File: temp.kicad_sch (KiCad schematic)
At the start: 0 parts

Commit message: can transceiver; power; mcu
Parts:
- added C19, C20, C21, C22, C23, C24: 100nF, symbol Device:C
- added D3, D4, D5, D6, D7, D8: BAT54A, Package_TO_SOT_SMD:SOT-23, symbol Diode:BAT54A
- added R53, R55, R57, R59, R61, R63: 680, symbol Device:R
- added R54, R56, R58, R60, R62, R64: 1k, symbol Device:R
- added R65, R66, R67, R68, R69, R70: 10k, symbol Device:R
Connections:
- new net +3.3VA: R53.1, R55.1, R57.1, R59.1, R61.1, R63.1, R65.2, R66.2, R67.2, R68.2, R69.2, R70.2
- new net GNDA: C19.2, C20.2, C21.2, C22.2, C23.2, C24.2
- new net TEMP1: C19.1, R54.2
- new net TEMP2: C20.1, R56.2
- new net TEMP3: C21.1, R58.2
- new net TEMP5: C22.1, R60.2
- new net TEMP6: C23.1, R62.2
- new net TEMP7: C24.1, R64.2
- new net TEMP_HOT: D3.3, D4.3, D5.3, D6.3, D7.3, D8.3, R65.1, R66.1, R67.1, R68.1, R69.1, R70.1
- new net TENSE3: D4.2
- new net TENSE6: D7.2
- new net TSENSE1: D3.1, R53.2, R54.1
- new net TSENSE2: D3.2, D4.1, R55.2, R56.1
- new net TSENSE3: D5.1, R57.2, R58.1
- new net TSENSE4: D5.2, D6.1, R59.2, R60.1
- new net TSENSE5: D6.2, D7.1, R61.2, R62.1
- new net TSENSE6: D8.1, R63.2, R64.1
- new net TSENSE7: D8.2

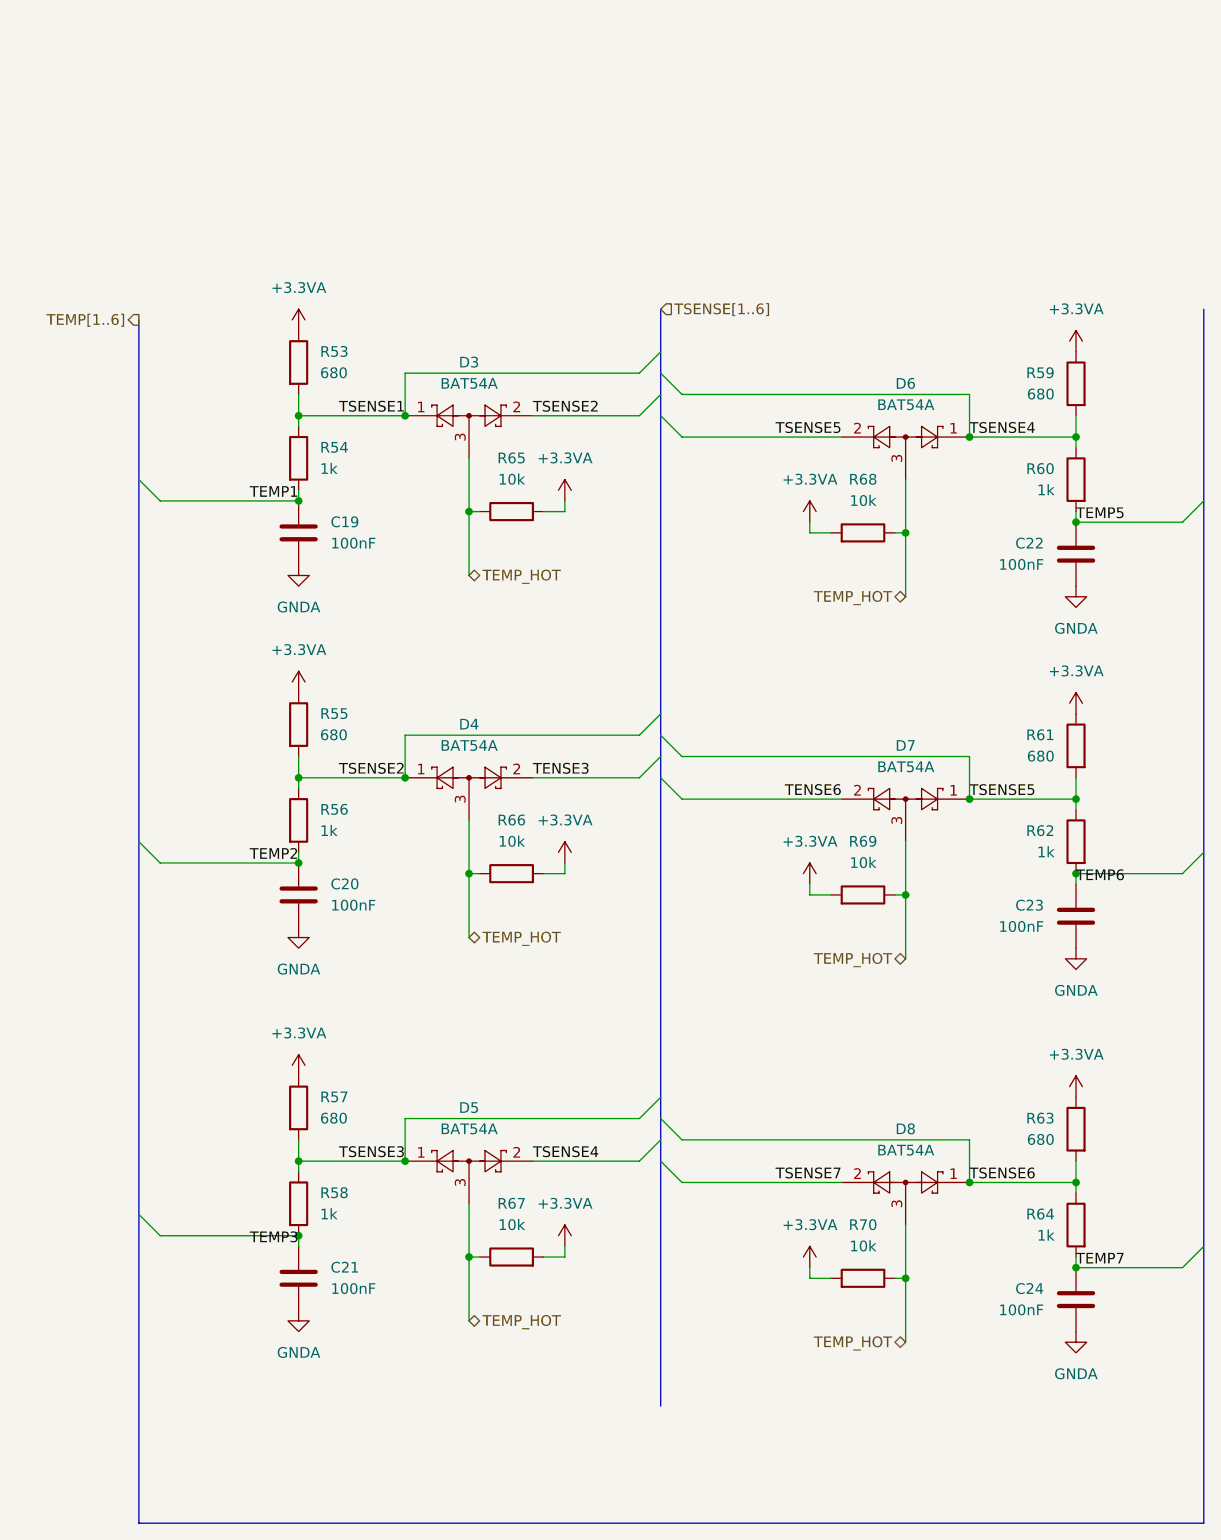
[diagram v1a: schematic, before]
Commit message: Add presentation (slides, PDF, pptx) and latest schematic edits
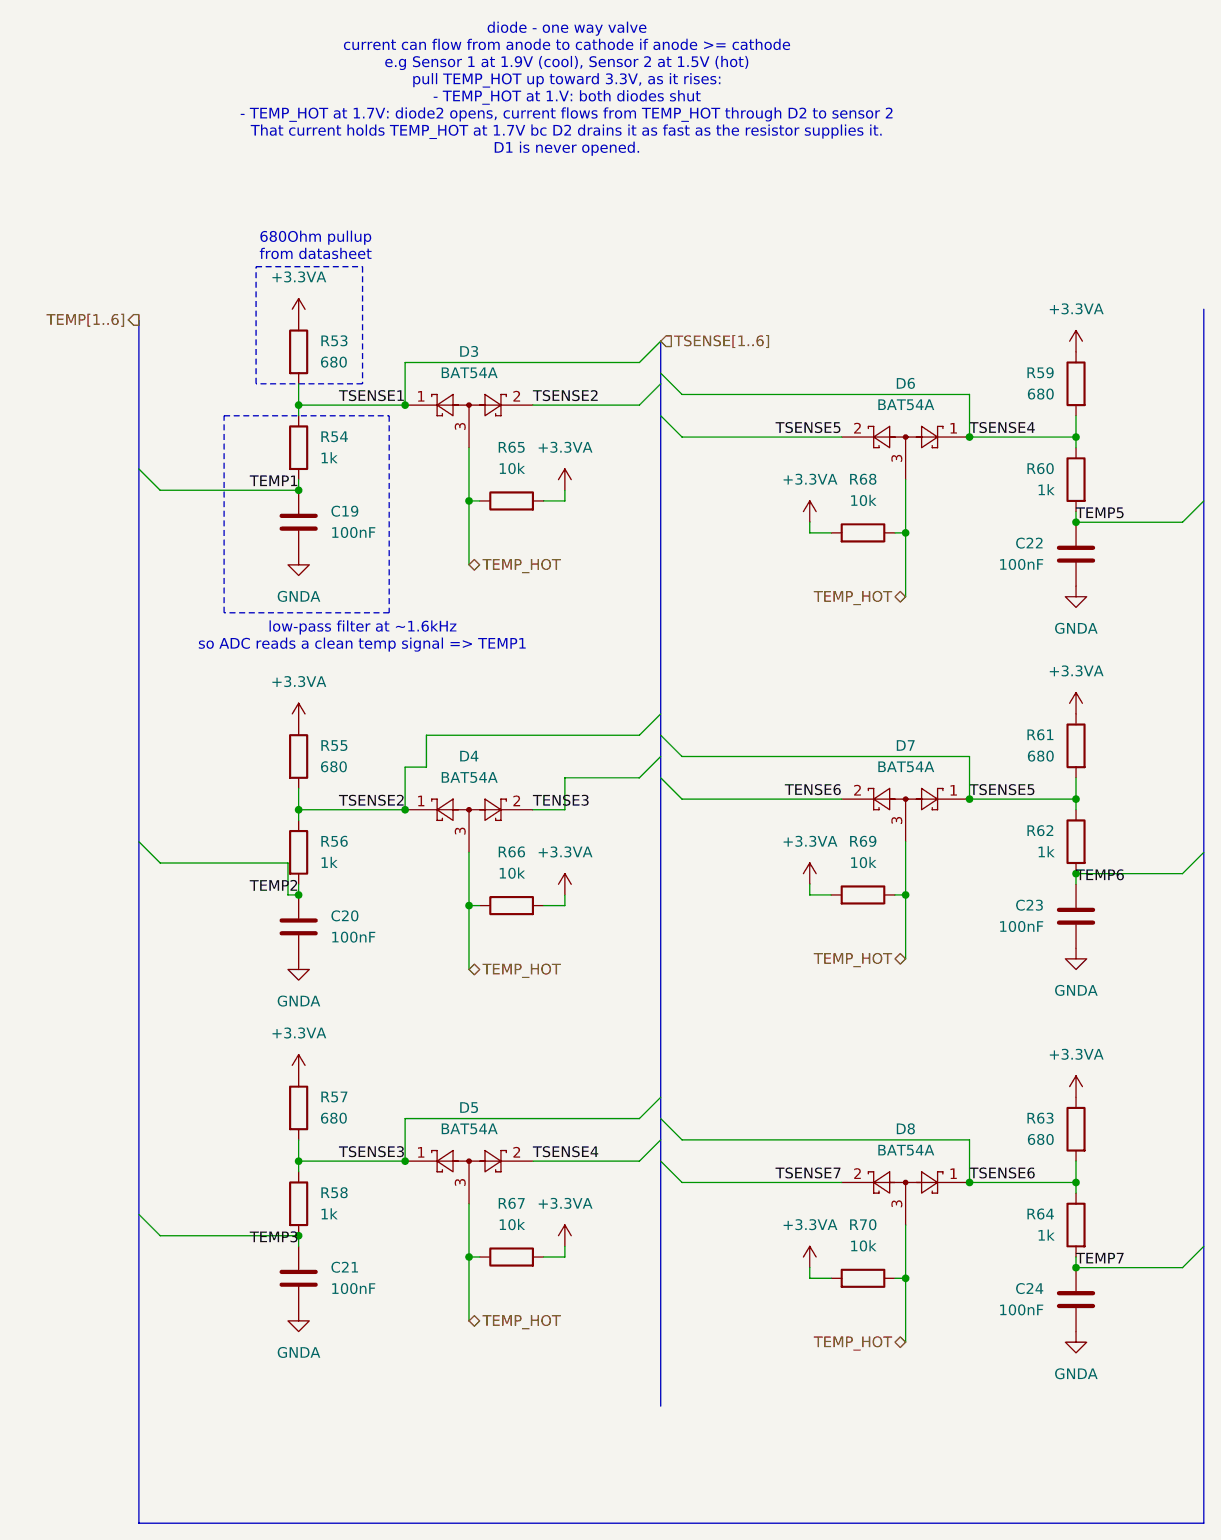
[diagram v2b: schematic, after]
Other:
- note added: "680Ohm pullup from datasheet"
- note added: "diode - one way valve current can flow from anode to cathode if anode >= cathode e.g Sensor 1 at 1.9V (cool), Sensor 2 at 1.5V (hot) pull TEMP_HOT up toward 3.3V, as it rises: - TEMP_HOT at 1.V: both diodes shut - TEMP_HOT at 1.7V: diode2 opens, current flows from TEMP_HOT through D2 to sensor 2 That current holds TEMP_HOT at 1.7V bc D2 drains it as fast as the resistor supplies it. D1 is never o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"
- note added: "low-pass filter at ~1.6kHz so ADC reads a clean temp signal => TEMP1"
- moved on the sheet: C19, C20, D3, D4, R53, R54, R55, R56, R65, R66
